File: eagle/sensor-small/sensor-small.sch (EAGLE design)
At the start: 13 parts, among them M1 NRF24-MODULE, U1 MSP430G2553IPW20, U3 SI7021, X1 1X05_1.27MM, X2 RENATA_SMTU2032-1

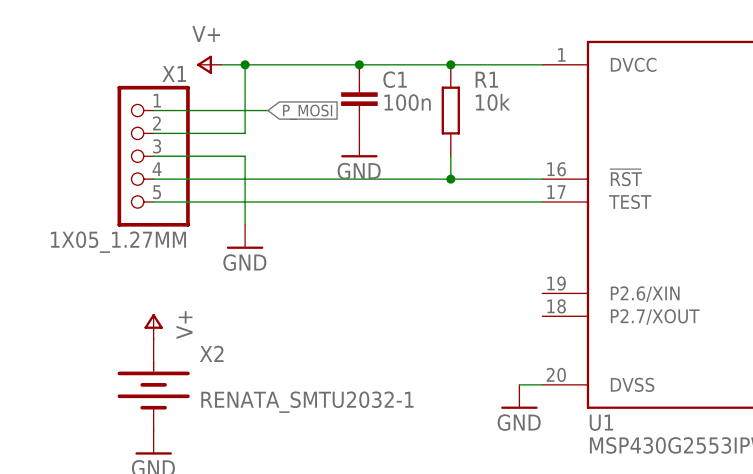
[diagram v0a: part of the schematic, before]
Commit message: Fixed swapped RST and TEST line in EAGLE design
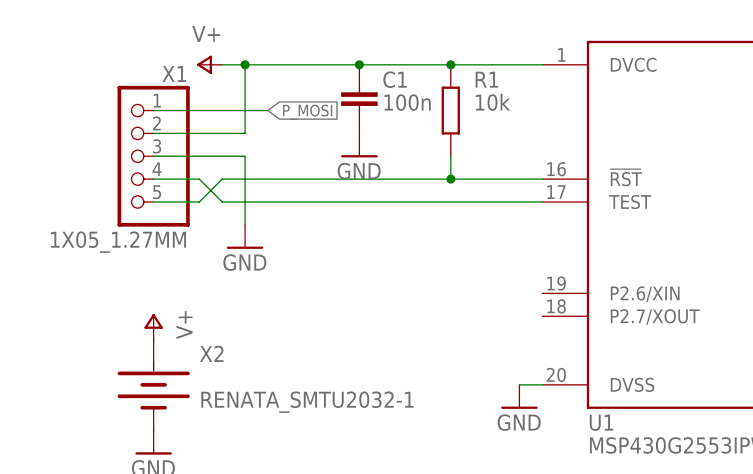
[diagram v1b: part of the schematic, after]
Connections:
- net N$2: now also X1.5; no longer X1.4
- net N$3: now also X1.4; no longer X1.5
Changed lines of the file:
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@@
 <wire x1="30.48" y1="53.34" x2="20.32" y2="53.34" width="0.1524" layer="91"/>
 <pinref part="R1" gate="G$1" pin="1"/>
-<wire x1="20.32" y1="53.34" x2="-12.7" y2="53.34" width="0.1524" layer="91"/>
 <wire x1="20.32" y1="55.88" x2="20.32" y2="53.34" width="0.1524" layer="91"/>
+<wire x1="20.32" y1="53.34" x2="-5.08" y2="53.34" width="0.1524" layer="91"/>
 <junction x="20.32" y="53.34"/>
-<pinref part="X1" gate="G$1" pin="4"/>
-</segment>
-</net>
-<net name="N$3" class="0">
-<segment>
-<pinref part="U1" gate="G$1" pin="TEST"/>
-<wire x1="30.48" y1="50.8" x2="-12.7" y2="50.8" width="0.1524" layer="91"/>
+<wire x1="-5.08" y1="53.34" x2="-7.62" y2="50.8" width="0.1524" layer="91"/>
 <pinref part="X1" gate="G$1" pin="5"/>
+<wire x1="-7.62" y1="50.8" x2="-12.7" y2="50.8" width="0.1524" layer="91"/>
 </segment>
 </net>
@@
 </segment>
 </net>
+<net name="N$3" class="0">
+<segment>
+<pinref part="X1" gate="G$1" pin="4"/>
+<wire x1="-12.7" y1="53.34" x2="-7.62" y2="53.34" width="0.1524" layer="91"/>
+<wire x1="-7.62" y1="53.34" x2="-5.08" y2="50.8" width="0.1524" layer="91"/>
+<pinref part="U1" gate="G$1" pin="TEST"/>
+<wire x1="-5.08" y1="50.8" x2="30.48" y2="50.8" width="0.1524" layer="91"/>
+</segment>
+</net>

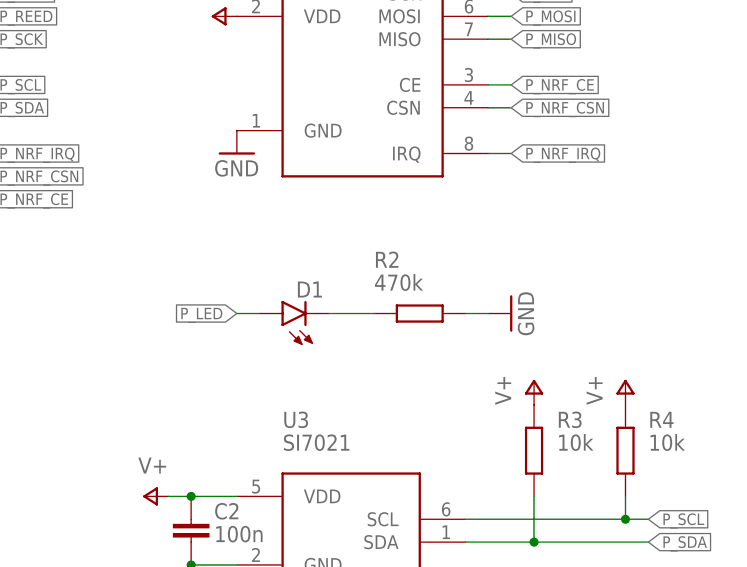
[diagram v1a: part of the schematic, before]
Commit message: Changed LED resistor value
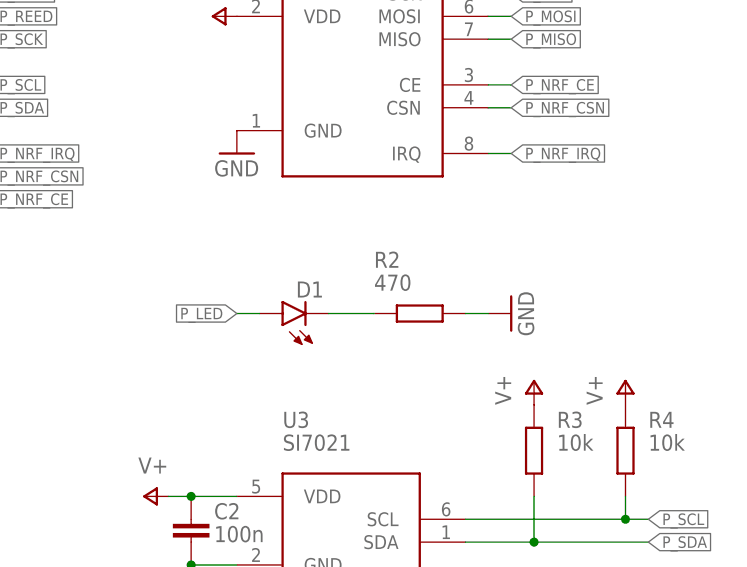
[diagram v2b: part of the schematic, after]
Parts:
- R2: value 470k -> 470
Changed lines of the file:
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@@
 <part name="P+2" library="supply1" library_urn="urn:adsk.eagle:library:371" deviceset="V+" device=""/>
 <part name="GND4" library="supply1" library_urn="urn:adsk.eagle:library:371" deviceset="GND" device=""/>
-<part name="R2" library="rfr-lib-passive" deviceset="R" device="0603" value="470k"/>
+<part name="R2" library="rfr-lib-passive" deviceset="R" device="0603" value="470"/>
 <part name="D1" library="led" library_urn="urn:adsk.eagle:library:259" deviceset="LED" device="CHIPLED_0805" package3d_urn="urn:adsk.eagle:package:15821/2"/>
 <part name="GND5" library="supply1" library_urn="urn:adsk.eagle:library:371" deviceset="GND" device=""/>
